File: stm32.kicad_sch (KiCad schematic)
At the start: 2 parts, among them U6 STM32G431RBIx

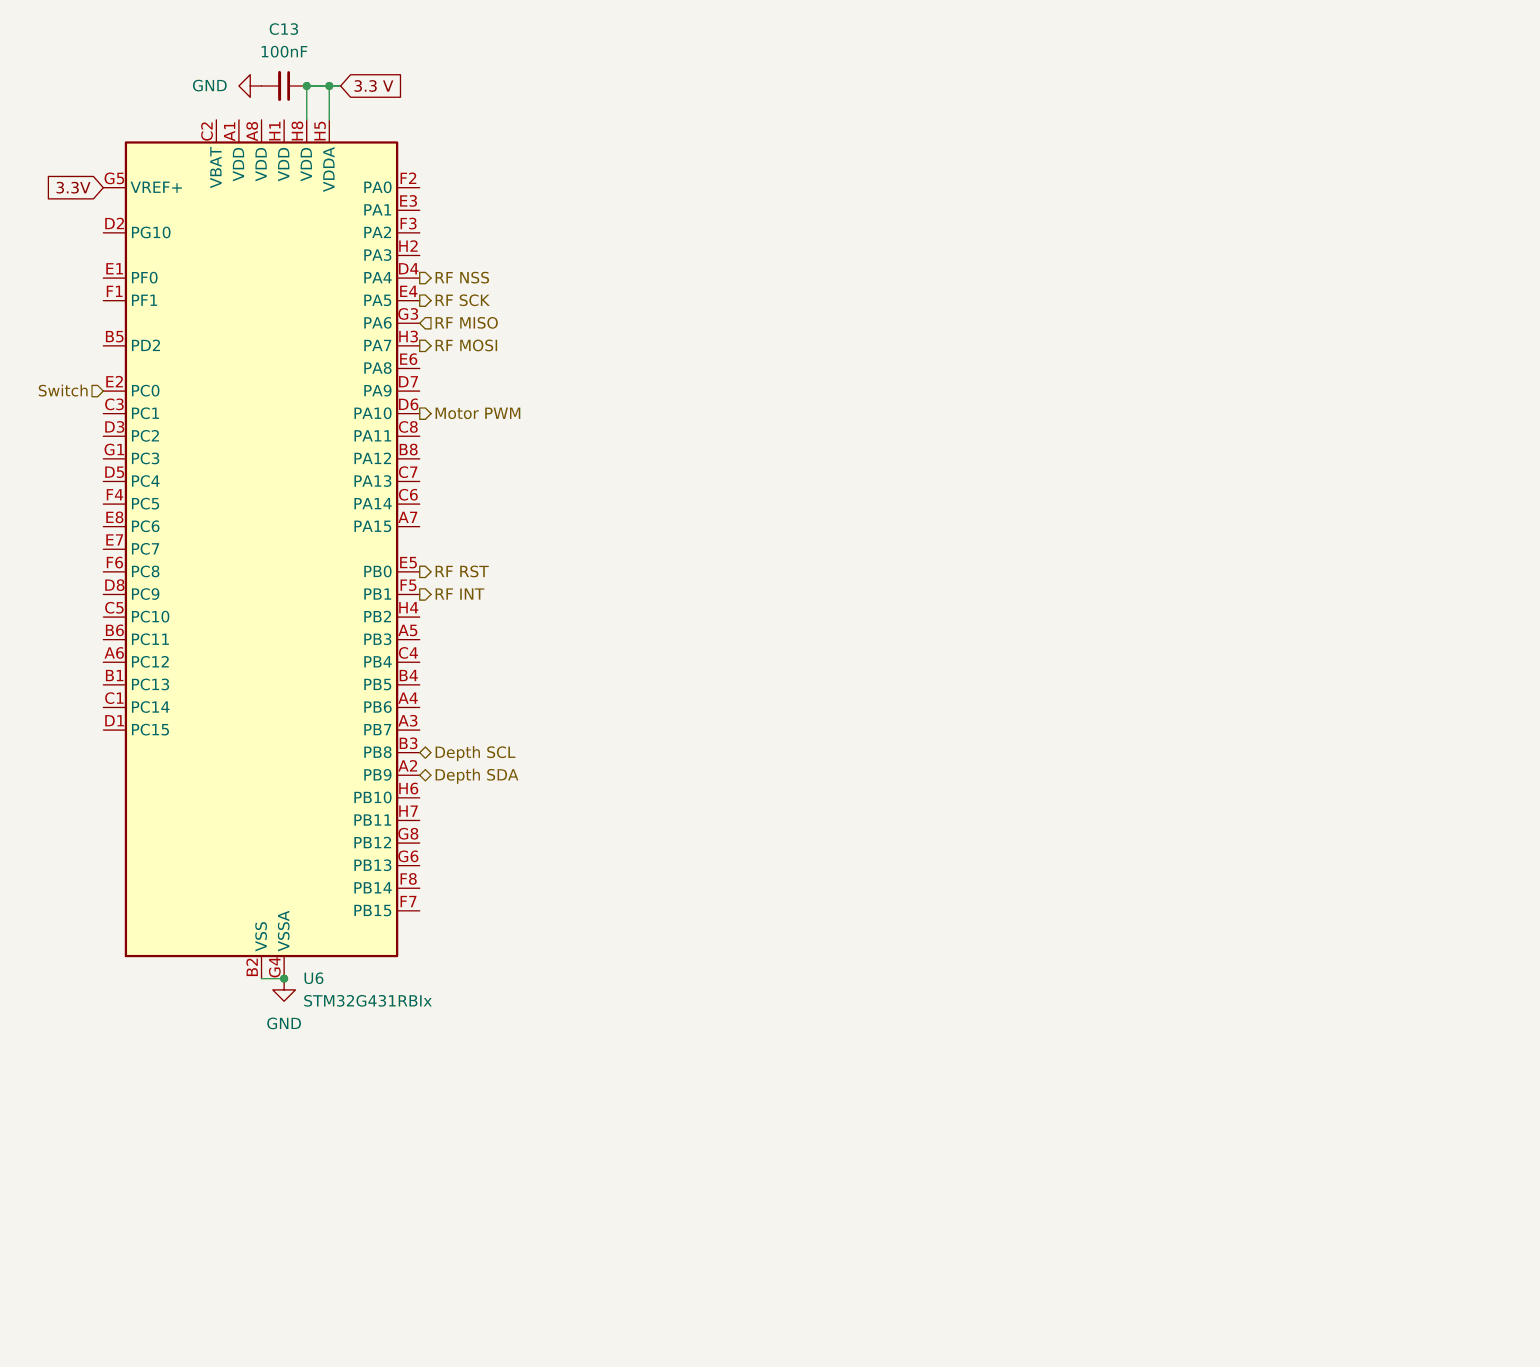
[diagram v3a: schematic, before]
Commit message: Corrected stm32 symbol
made corrections to the stm32 for the package and the schmeatic
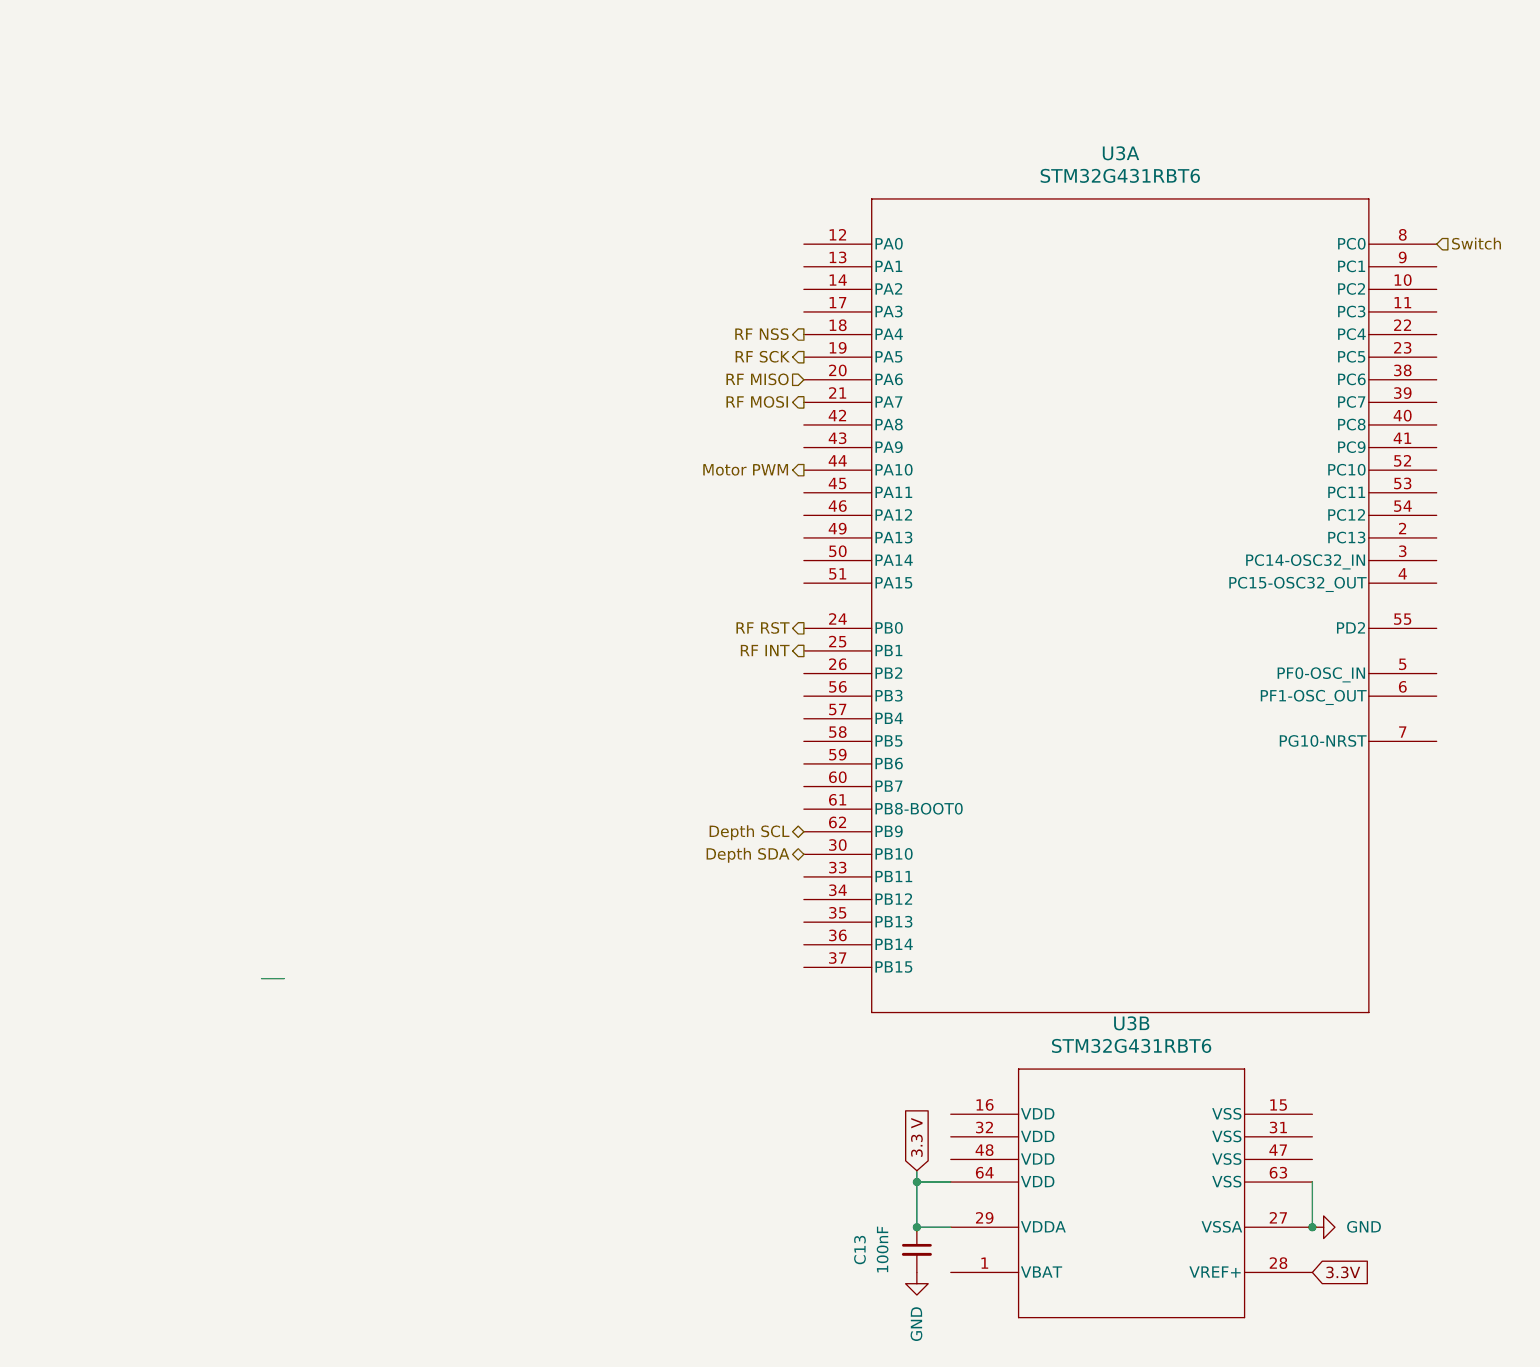
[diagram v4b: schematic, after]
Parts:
- removed U6: STM32G431RBIx, Package_BGA:UFBGA-64_5x5mm_Layout8x8_P0.5mm, symbol MCU_ST_STM32G4:STM32G431RBIx
- added U3: STM32G431RBT6, LQFP64-10x10mm, symbol stm32:STM32G431RBT6
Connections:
- net 3.3 V: now also U3.29 (VDDA), U3.64 (VDD)
- net 3.3V: now also U3.28 (VREF+)
- net Depth SCL: now also U3.62 (PB9)
- net Depth SDA: now also U3.30 (PB10)
- net GND: now also U3.27 (VSSA), U3.63 (VSS)
- net Motor PWM: now also U3.44 (PA10)
- net RF INT: now also U3.25 (PB1)
- net RF MISO: now also U3.20 (PA6)
- net RF MOSI: now also U3.21 (PA7)
- net RF NSS: now also U3.18 (PA4)
- net RF RST: now also U3.24 (PB0)
- net RF SCK: now also U3.19 (PA5)
- net Switch: now also U3.8 (PC0)

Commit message: Modifications to power system to support what is required
modified
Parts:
- U3: footprint LQFP64-10x10mm -> stm32:LQFP64-10x10mm
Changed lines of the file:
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@@
 			)
 		)
-		(property "Footprint" "LQFP64-10x10mm"
+		(property "Footprint" "stm32:LQFP64-10x10mm"
 			(at 116.84 134.62 0)
 			(hide yes)
@@
 			)
 		)
-		(property "Footprint" "LQFP64-10x10mm"
+		(property "Footprint" "stm32:LQFP64-10x10mm"
 			(at 100.33 36.83 0)
 			(hide yes)

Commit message: USB-C + Complete wiring
Compltetly wired the pcb (I don't understand the DRC errors) and added a usb C to flash the stm, modified the switch to be the BOOT0 for the stm so it controls whether the stm is in flash mode
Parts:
- added R_PD_USBC_0: 5.1kΩ, Resistor_SMD:R_0603_1608Metric, symbol Device:R_Small_US
- added R_PD_USBC_1: 5.1k, Resistor_SMD:R_0603_1608Metric, symbol Device:R_Small_US
- added R_USBC_DIV0: 20kΩ, Resistor_SMD:R_0603_1608Metric, symbol Device:R_Small_US
- added R_USBC_DIV1: 10kΩ, Resistor_SMD:R_0603_1608Metric, symbol Device:R_Small_US
- added usb_c: USB_C_Receptacle_USB2.0_16P, symbol Connector:USB_C_Receptacle_USB2.0_16P
- renumbered C13 to C_D_STM1
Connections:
- net 3.3V is gone; now on net 3.3 V: U3.28 (VREF+)
- net GND: now also R_PD_USBC_0.2, R_PD_USBC_1.2, R_USBC_DIV1.2, usb_c.A1 (GND), usb_c.A12 (GND), usb_c.B1 (GND), usb_c.B12 (GND), usb_c.SH (SHIELD)
- net Switch: now also U3.61 (PB8-BOOT0); no longer U3.8 (PC0)
- net at U3.17 (PA3): now also R_USBC_DIV0.2, R_USBC_DIV1.1
- net at U3.45 (PA11): now also usb_c.A7 (D-), usb_c.B7 (D-)
- net at U3.46 (PA12): now also usb_c.A6 (D+), usb_c.B6 (D+)
- new net: R_PD_USBC_1.1, usb_c.B5 (CC2)
- new net: R_PD_USBC_0.1, usb_c.A5 (CC1)
- new net: R_USBC_DIV0.1, usb_c.A4 (VBUS), usb_c.A9 (VBUS), usb_c.B4 (VBUS), usb_c.B9 (VBUS)

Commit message: Checkpoint
Checkpoint, pre battery telemetry, pre new stm
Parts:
- removed R_PD_USBC_0: 5.1kΩ, Resistor_SMD:R_0603_1608Metric, symbol Device:R_Small_US
- removed usb_c: USB_C_Receptacle_USB2.0_16P, symbol Connector:USB_C_Receptacle_USB2.0_16P
- added J1: USB4220-03-1040-C_REVA, usbc:GCT_USB4220-03-1040-C_REVA, symbol usbc:USB4220-03-1040-C_REVA
- added R_PD_USBC_2: 5.1kΩ, Resistor_SMD:R_0603_1608Metric, symbol Device:R_Small_US
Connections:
- net GND: now also J1.A1 (GND_A), J1.A12 (GND_A), J1.B1 (GND_B), J1.B12 (GND_A), J1.S1 (SHIELD), J1.S2 (SHIELD), J1.S3 (SHIELD), J1.S4 (SHIELD), R_PD_USBC_2.1
- net at R_PD_USBC_1.1: now also J1.B5 (CC2)
- net VBUS_A: now reaches R_USBC_DIV0.1
- net VBUS_A: now also J1.A4 (VBUS_A), J1.A9 (VBUS_A)
- net at U3.46 (PA12): now also J1.B6 (DP2)
- net at U3.45 (PA11): now also J1.B7 (DN2)
- new net: J1.A5 (CC1), R_PD_USBC_2.2
- new net VBUS_B: J1.B4 (VBUS_B), J1.B9 (VBUS_B)

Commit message: Update
Update
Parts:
- removed J1: USB4220-03-1040-C_REVA, usbc:GCT_USB4220-03-1040-C_REVA, symbol usbc:USB4220-03-1040-C_REVA
- removed R_PD_USBC_1: 5.1k, Resistor_SMD:R_0603_1608Metric, symbol Device:R_Small_US
- removed R_PD_USBC_2: 5.1kΩ, Resistor_SMD:R_0603_1608Metric, symbol Device:R_Small_US
- removed R_USBC_DIV0: 20kΩ, Resistor_SMD:R_0603_1608Metric, symbol Device:R_Small_US
- removed R_USBC_DIV1: 10kΩ, Resistor_SMD:R_0603_1608Metric, symbol Device:R_Small_US
- removed unit 1 of U3
- added C_D_STM2, C_D_STM3: 100nF, Capacitor_SMD:C_0603_1608Metric, symbol Device:C_Small
- added U2: STM32C542CCT6, LQFP48-7X7, symbol STM32:STM32C542CCT6
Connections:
- net 3.3 V: now also C_D_STM2.2, C_D_STM3.1, U2.24 (VDD), U2.48 (VDD), U2.9 (VREF+); no longer U3.28 (VREF+)
- net Depth SCL: now also U2.39 (PB3)
- net Depth SDA: now also U2.40 (PB4)
- net GND: now also C_D_STM2.1, C_D_STM3.2, U2.23 (VSS), U2.47 (VSS); no longer U3.27 (VSSA), U3.63 (VSS)
- net Motor PWM: now also U2.19 (PB1)
- net RF INT: now also U2.18 (PB0)
- net RF MISO: now also U2.15 (PA5)
- net RF MOSI: now also U2.16 (PA6)
- net RF NSS: now also U2.13 (PA3)
- net RF RST: now also U2.17 (PA7)
- net RF SCK: now also U2.14 (PA4)
- net Switch: now also U2.38 (PA15)
- new net: U3.27 (VSSA), U3.63 (VSS)
- new net INA ALERT: U2.41 (PB5)
- new net INA SCL: U2.42 (PB6)
- new net INA SDA: U2.43 (PB7)
- new net TMP ALERT: U2.10 (PA0)
- new net TMP SCL: U2.12 (PA2)
- new net TMP SDA: U2.11 (PA1)
- new net USB BUS: U2.33 (PA12)
- new net USB DN: U2.32 (PA11)
- new net USB DP: U2.31 (PA10)
